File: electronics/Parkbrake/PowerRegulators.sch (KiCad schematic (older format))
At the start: 23 parts

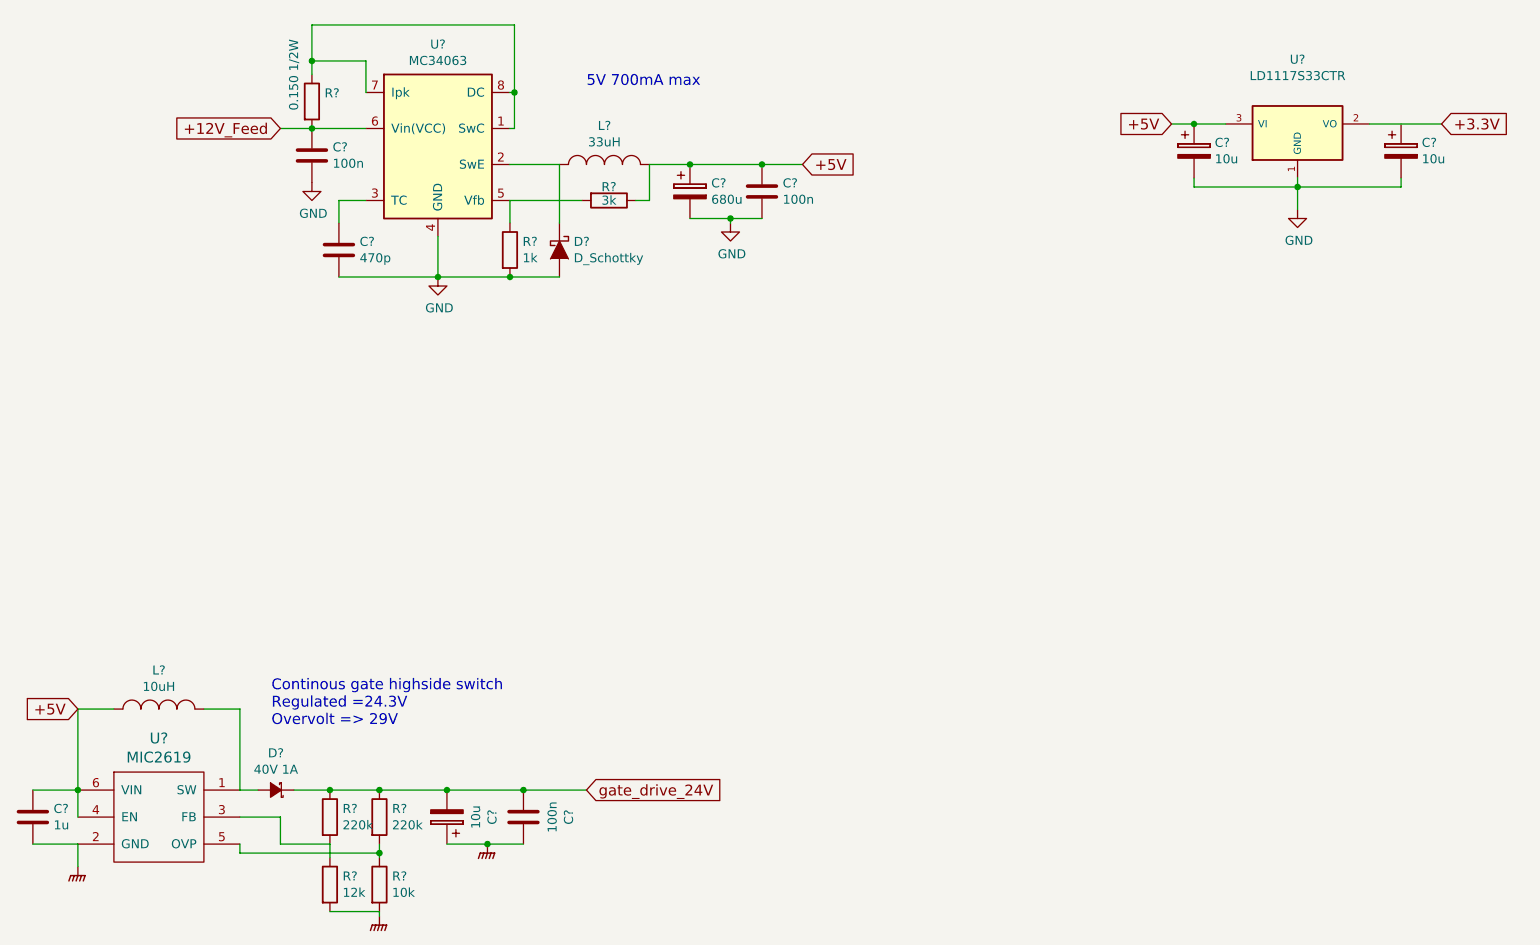
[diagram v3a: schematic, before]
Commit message: Make it pass DRC rule check
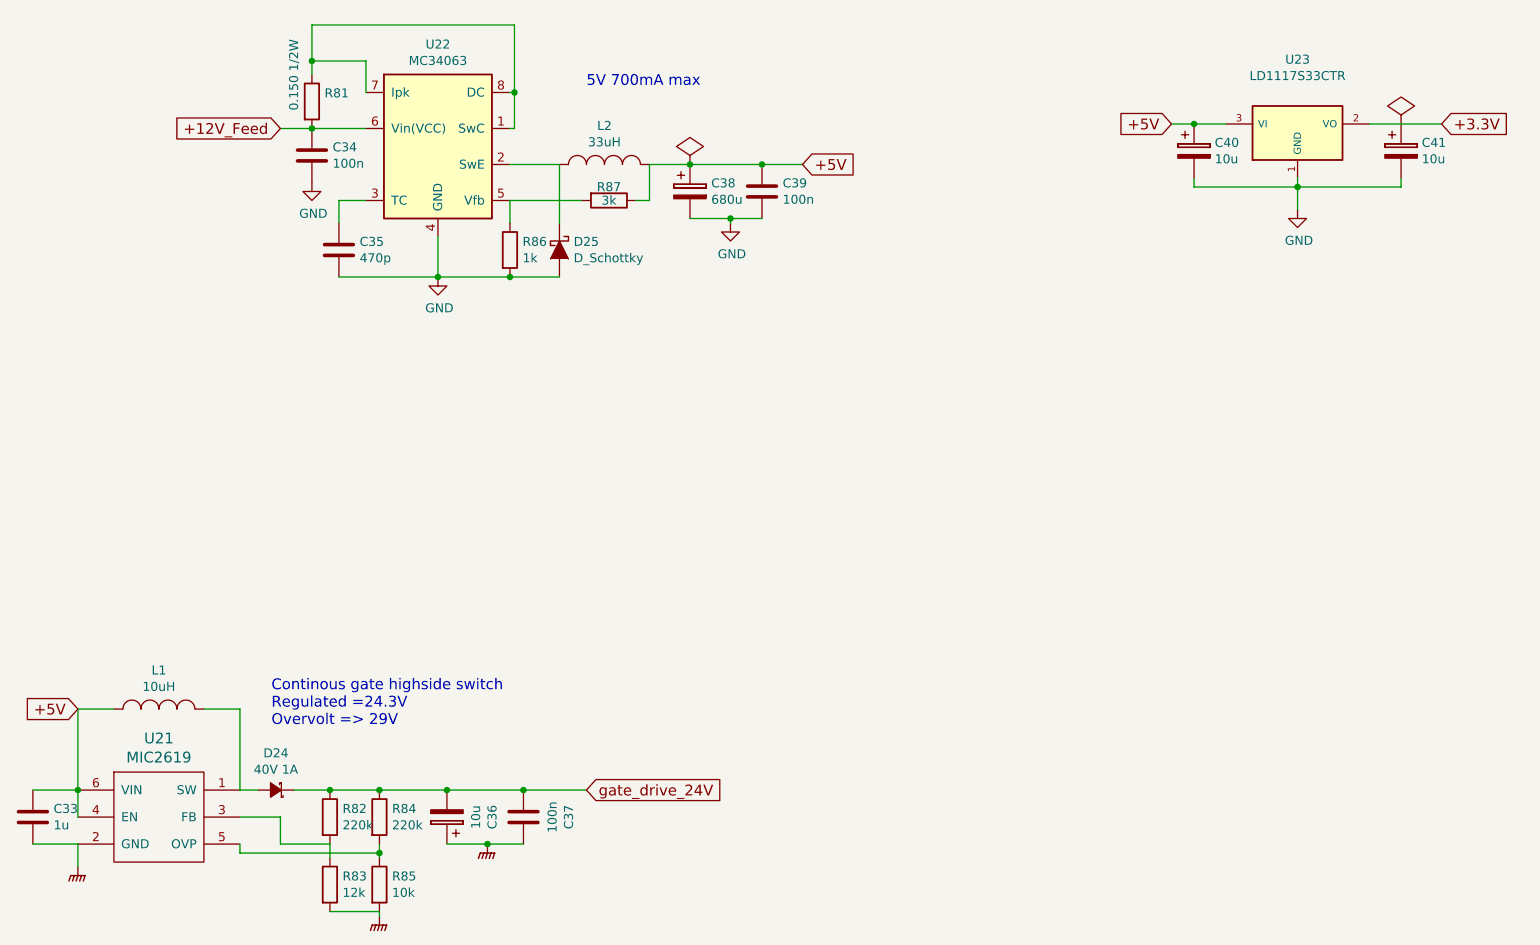
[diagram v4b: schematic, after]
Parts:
- gave numbers to parts that had none: 23
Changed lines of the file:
@@
 $EndDescr
 $Comp
-L MIC2619 U?
+L MIC2619 U21
 U 1 1 570107B3
 P 2125 6150
-F 0 "U?" H 2125 6587 60  0000 C CNN
+F 0 "U21" H 2125 6587 60  0000 C CNN
 F 1 "MIC2619" H 2125 6481 60  0000 C CNN
 F 2 "TO_SOT_Packages_SMD:SOT-23-6" H 2125 6150 60  0001 C CNN
@@
 +5V
 $Comp
-L C C?
+L C C33
 U 1 1 570109D3
 P 1425 6150
-F 0 "C?" H 1540 6196 50  0000 L CNN
+F 0 "C33" H 1540 6196 50  0000 L CNN
 F 1 "1u" H 1540 6105 50  0000 L CNN
 F 2 "Capacitors_SMD:C_1206" H 1463 6000 50  0001 C CNN
@@
 $EndComp
 $Comp
-L INDUCTOR_SMALL L?
+L INDUCTOR_SMALL L1
 U 1 1 57010A1F
 P 2125 5550
-F 0 "L?" H 2125 5765 50  0000 C CNN
+F 0 "L1" H 2125 5765 50  0000 C CNN
 F 1 "10uH" H 2125 5674 50  0000 C CNN
 F 2 "Inductors:Inductor_1212" H 2125 5550 50  0001 C CNN
@@
 $EndComp
 $Comp
-L CP C?
+L CP C36
 U 1 1 57010AEF
 P 3725 6150
-F 0 "C?" V 3473 6150 50  0000 C CNN
+F 0 "C36" V 3473 6150 50  0000 C CNN
 F 1 "10u" V 3564 6150 50  0000 C CNN
 F 2 "Capacitors_SMD:c_elec_5x5.3" H 3763 6000 50  0001 C CNN
@@
 $EndComp
 $Comp
-L GNDPWR #PWR?
+L GNDPWR #PWR064
 U 1 1 57010C16
 P 1675 6425
-F 0 "#PWR?" H 1675 6225 50  0001 C CNN
+F 0 "#PWR064" H 1675 6225 50  0001 C CNN
 F 1 "GNDPWR" H 1675 6200 50  0001 C CNN
 F 2 "" H 1675 6375 50  0000 C CNN
@@
 $EndComp
 $Comp
-L D_Schottky_Small D?
+L D_Schottky_Small D24
 U 1 1 57010E55
 P 2775 6000
-F 0 "D?" H 2775 5795 50  0000 C CNN
+F 0 "D24" H 2775 5795 50  0000 C CNN
 F 1 "40V 1A" H 2775 5886 50  0000 C CNN
 F 2 "Diodes_SMD:DO-214AB" V 2775 6000 50  0001 C CNN
@@
 $EndComp
 $Comp
-L R R?
+L R R82
 U 1 1 57010F19
 P 3075 6150
-F 0 "R?" H 3145 6196 50  0000 L CNN
+F 0 "R82" H 3145 6196 50  0000 L CNN
 F 1 "220k" H 3145 6105 50  0000 L CNN
 F 2 "Resistors_SMD:R_0805" V 3005 6150 50  0001 C CNN
@@
 $EndComp
 $Comp
-L R R?
+L R R83
 U 1 1 57010F4F
 P 3075 6525
-F 0 "R?" H 3145 6571 50  0000 L CNN
+F 0 "R83" H 3145 6571 50  0000 L CNN
 F 1 "12k" H 3145 6480 50  0000 L CNN
 F 2 "Resistors_SMD:R_0805" V 3005 6525 50  0001 C CNN
@@
 $EndComp
 $Comp
-L R R?
+L R R84
 U 1 1 57011141
 P 3350 6150
-F 0 "R?" H 3420 6196 50  0000 L CNN
+F 0 "R84" H 3420 6196 50  0000 L CNN
 F 1 "220k" H 3420 6105 50  0000 L CNN
 F 2 "Resistors_SMD:R_0805" V 3280 6150 50  0001 C CNN
@@
 $EndComp
 $Comp
-L R R?
+L R R85
 U 1 1 57011177
 P 3350 6525
-F 0 "R?" H 3420 6571 50  0000 L CNN
+F 0 "R85" H 3420 6571 50  0000 L CNN
 F 1 "10k" H 3420 6480 50  0000 L CNN
 F 2 "Resistors_SMD:R_0805" V 3280 6525 50  0001 C CNN
@@
 $EndComp
 $Comp
-L GNDPWR #PWR?
+L GNDPWR #PWR065
 U 1 1 57011519
 P 3350 6700
-F 0 "#PWR?" H 3350 6500 50  0001 C CNN
+F 0 "#PWR065" H 3350 6500 50  0001 C CNN
 F 1 "GNDPWR" H 3357 6774 50  0001 C CNN
 F 2 "" H 3350 6650 50  0000 C CNN
@@
 $EndComp
 $Comp
-L GNDPWR #PWR?
+L GNDPWR #PWR066
 U 1 1 57011573
 P 3950 6300
-F 0 "#PWR?" H 3950 6100 50  0001 C CNN
+F 0 "#PWR066" H 3950 6100 50  0001 C CNN
 F 1 "GNDPWR" H 3957 6374 50  0001 C CNN
 F 2 "" H 3950 6250 50  0000 C CNN
@@
 Continous gate highside switch\nRegulated =24.3V\nOvervolt => 29V
 $Comp
-L C C?
+L C C37
 U 1 1 57010B62
 P 4150 6150
-F 0 "C?" V 3898 6150 50  0000 C CNN
+F 0 "C37" V 3898 6150 50  0000 C CNN
 F 1 "100n" V 3989 6150 50  0000 C CNN
 F 2 "Capacitors_SMD:C_0805" H 4188 6000 50  0001 C CNN
@@
 P 3675 2425
 AR Path="/57089F7E" Ref="U?"  Part="1"
-AR Path="/57088F10/57089F7E" Ref="U?"  Part="1"
-F 0 "U?" H 3675 2992 50  0000 C CNN
+AR Path="/57088F10/57089F7E" Ref="U22"  Part="1"
+F 0 "U22" H 3675 2992 50  0000 C CNN
 F 1 "MC34063" H 3675 2901 50  0000 C CNN
 F 2 "Housings_SOIC:SOIC-8_3.9x4.9mm_Pitch1.27mm" H 3675 2901 50  0001 C CNN
@@
 $EndComp
 $Comp
-L GND #PWR?
+L GND #PWR067
 U 1 1 5708A002
 P 3675 3150
-F 0 "#PWR?" H 3675 2900 50  0001 C CNN
+F 0 "#PWR067" H 3675 2900 50  0001 C CNN
 F 1 "GND" H 3683 2977 50  0000 C CNN
 F 2 "" H 3675 3150 50  0000 C CNN
@@
 $EndComp
 $Comp
-L C C?
+L C C35
 U 1 1 5708A058
 P 3125 3000
-F 0 "C?" H 3240 3046 50  0000 L CNN
+F 0 "C35" H 3240 3046 50  0000 L CNN
 F 1 "470p" H 3240 2955 50  0000 L CNN
 F 2 "Capacitors_SMD:C_0805" H 3163 2850 50  0001 C CNN
@@
 $EndComp
 $Comp
-L R R?
+L R R86
 U 1 1 5708A132
 P 4075 3000
-F 0 "R?" H 4145 3046 50  0000 L CNN
+F 0 "R86" H 4145 3046 50  0000 L CNN
 F 1 "1k" H 4145 2955 50  0000 L CNN
 F 2 "Resistors_SMD:R_0805" V 4005 3000 50  0001 C CNN
@@
 $EndComp
 $Comp
-L R R?
+L R R87
 U 1 1 5708A176
 P 4625 2725
-F 0 "R?" V 4550 2725 50  0000 C CNN
+F 0 "R87" V 4550 2725 50  0000 C CNN
 F 1 "3k" V 4625 2725 50  0000 C CNN
 F 2 "Resistors_SMD:R_0805" V 4555 2725 50  0001 C CNN
@@
 $EndComp
 $Comp
-L R R?
+L R R81
 U 1 1 5708A1CB
 P 2975 2175
-F 0 "R?" H 3045 2221 50  0000 L CNN
+F 0 "R81" H 3045 2221 50  0000 L CNN
 F 1 "0.150 1/2W" V 2875 2125 50  0000 L CNN
 F 2 "Resistors_SMD:R_1206" V 2905 2175 50  0001 C CNN
@@
 $EndComp
 $Comp
-L INDUCTOR_SMALL L?
+L INDUCTOR_SMALL L2
 U 1 1 5708A258
 P 4600 2525
-F 0 "L?" H 4600 2740 50  0000 C CNN
+F 0 "L2" H 4600 2740 50  0000 C CNN
 F 1 "33uH" H 4600 2649 50  0000 C CNN
 F 2 "Inductors:SELF-WE-PD-XXL" H 4600 2525 50  0001 C CNN
@@
 $EndComp
 $Comp
-L D_Schottky D?
+L D_Schottky D25
 U 1 1 5708A2E4
 P 4350 3000
-F 0 "D?" V 4304 3079 50  0000 L CNN
+F 0 "D25" V 4304 3079 50  0000 L CNN
 F 1 "D_Schottky" V 4395 3079 50  0000 L CNN
 F 2 "Diodes_SMD:DO-214AB" H 4350 3000 50  0001 C CNN
@@
 $EndComp
 $Comp
-L CP C?
+L CP C38
 U 1 1 5708AB53
 P 5075 2675
-F 0 "C?" H 5193 2721 50  0000 L CNN
+F 0 "C38" H 5193 2721 50  0000 L CNN
 F 1 "680u" H 5193 2630 50  0000 L CNN
 F 2 "Capacitors_SMD:c_elec_10x10.5" H 5113 2525 50  0001 C CNN
@@
 $EndComp
 $Comp
-L GND #PWR?
+L GND #PWR068
 U 1 1 5708ABA3
 P 5300 2850
-F 0 "#PWR?" H 5300 2600 50  0001 C CNN
+F 0 "#PWR068" H 5300 2600 50  0001 C CNN
 F 1 "GND" H 5308 2677 50  0000 C CNN
 F 2 "" H 5300 2850 50  0000 C CNN
@@
 $EndComp
 $Comp
-L C C?
+L C C39
 U 1 1 5708ABDB
 P 5475 2675
-F 0 "C?" H 5590 2721 50  0000 L CNN
+F 0 "C39" H 5590 2721 50  0000 L CNN
 F 1 "100n" H 5590 2630 50  0000 L CNN
 F 2 "Capacitors_SMD:C_0805" H 5513 2525 50  0001 C CNN
@@
 $EndComp
 $Comp
-L C C?
+L C C34
 U 1 1 5708B842
 P 2975 2475
-F 0 "C?" H 3090 2521 50  0000 L CNN
+F 0 "C34" H 3090 2521 50  0000 L CNN
 F 1 "100n" H 3090 2430 50  0000 L CNN
 F 2 "Capacitors_SMD:C_0805" H 3013 2325 50  0001 C CNN
@@
 $EndComp
 $Comp
-L GND #PWR?
+L GND #PWR069
 U 1 1 5708B974
 P 2975 2625
-F 0 "#PWR?" H 2975 2375 50  0001 C CNN
+F 0 "#PWR069" H 2975 2375 50  0001 C CNN
 F 1 "GND" H 2983 2452 50  0000 C CNN
 F 2 "" H 2975 2625 50  0000 C CNN
@@
 5V 700mA max
 $Comp
-L LD1117S33CTR U?
+L LD1117S33CTR U23
 U 1 1 5708D2D2
 P 8450 2350
-F 0 "U?" H 8450 2758 50  0000 C CNN
+F 0 "U23" H 8450 2758 50  0000 C CNN
 F 1 "LD1117S33CTR" H 8450 2667 50  0000 C CNN
 F 2 "TO_SOT_Packages_SMD:SOT-223" H 8450 2576 50  0001 C CNN
@@
 $EndComp
 $Comp
-L CP C?
+L CP C40
 U 1 1 5708D4A0
 P 7875 2450
-F 0 "C?" H 7990 2496 50  0000 L CNN
+F 0 "C40" H 7990 2496 50  0000 L CNN
 F 1 "10u" H 7990 2405 50  0000 L CNN
 F 2 "Capacitors_SMD:c_elec_5x5.3" H 7913 2300 50  0001 C CNN
@@
 $EndComp
 $Comp
-L CP C?
+L CP C41
 U 1 1 5708D4FA
 P 9025 2450
-F 0 "C?" H 9140 2496 50  0000 L CNN
+F 0 "C41" H 9140 2496 50  0000 L CNN
 F 1 "10u" H 9140 2405 50  0000 L CNN
 F 2 "Capacitors_SMD:c_elec_5x5.3" H 9063 2300 50  0001 C CNN
@@
 $EndComp
 $Comp
-L GND #PWR?
+L GND #PWR070
 U 1 1 5708D552
 P 8450 2775
-F 0 "#PWR?" H 8450 2525 50  0001 C CNN
+F 0 "#PWR070" H 8450 2525 50  0001 C CNN
 F 1 "GND" H 8458 2602 50  0000 C CNN
 F 2 "" H 8450 2775 50  0000 C CNN
@@
 Text GLabel 9250 2300 2    60   Input ~ 0
 +3.3V
+$Comp
+L PWR_FLAG #FLG071
+U 1 1 57980F2B
+P 9025 2300
+F 0 "#FLG071" H 9025 2395 50  0001 C CNN
+F 1 "PWR_FLAG" H 9025 2480 50  0001 C CNN
+F 2 "" H 9025 2300 50  0000 C CNN
+F 3 "" H 9025 2300 50  0000 C CNN
+	1    9025 2300
+	1    0    0    -1
+$EndComp
+$Comp
+L PWR_FLAG #FLG072
+U 1 1 5798551D
+P 5075 2525
+F 0 "#FLG072" H 5075 2620 50  0001 C CNN
+F 1 "PWR_FLAG" H 5075 2705 50  0001 C CNN
+F 2 "" H 5075 2525 50  0000 C CNN
+F 3 "" H 5075 2525 50  0000 C CNN
+	1    5075 2525
+	1    0    0    -1
+$EndComp
 $EndSCHEMATC
